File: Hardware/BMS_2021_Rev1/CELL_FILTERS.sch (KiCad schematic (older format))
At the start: 54 parts

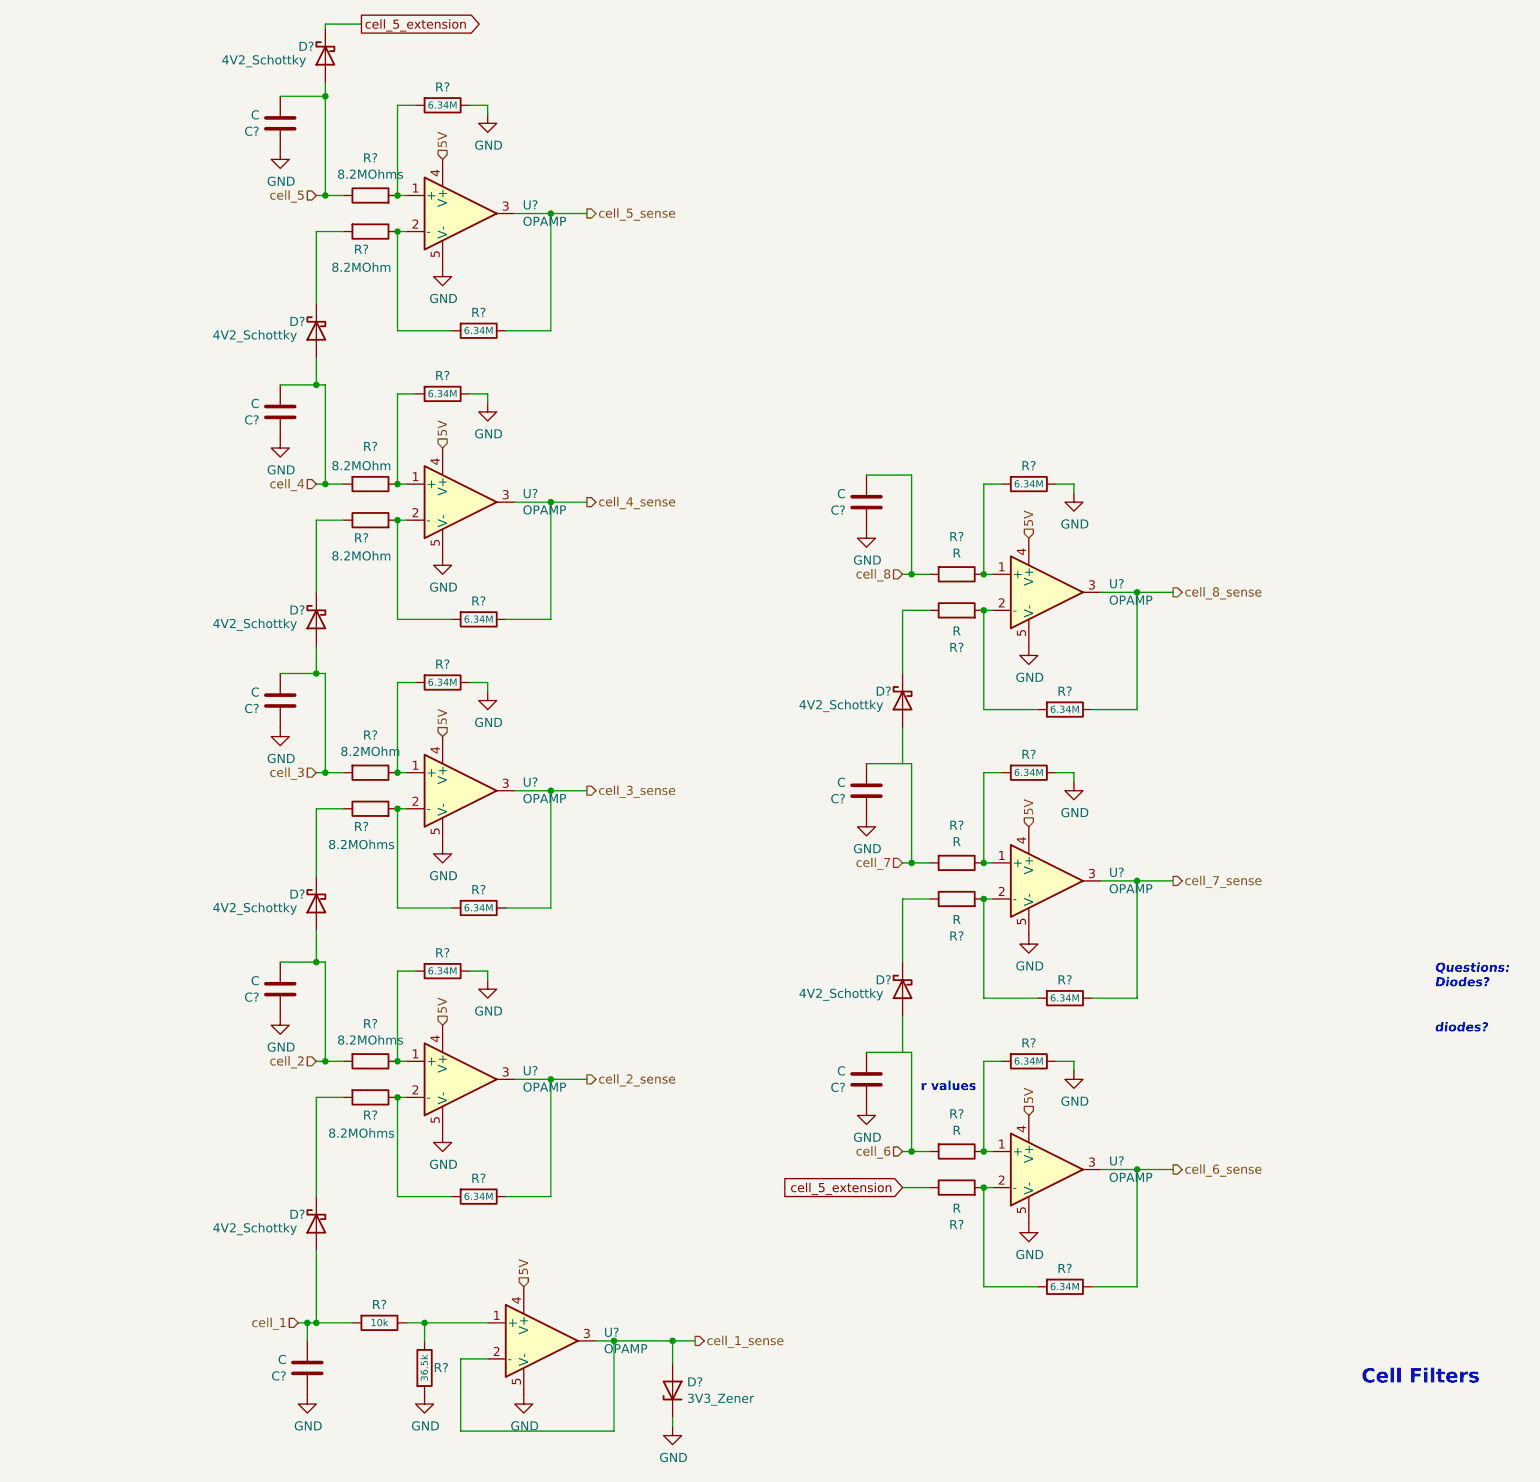
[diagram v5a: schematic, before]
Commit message: stuff added
-cellFilter IC and R values added
-MOSFET values added
-extra TIVA headers added
-currentSense R values labeled properly
-things are actually connected together this time
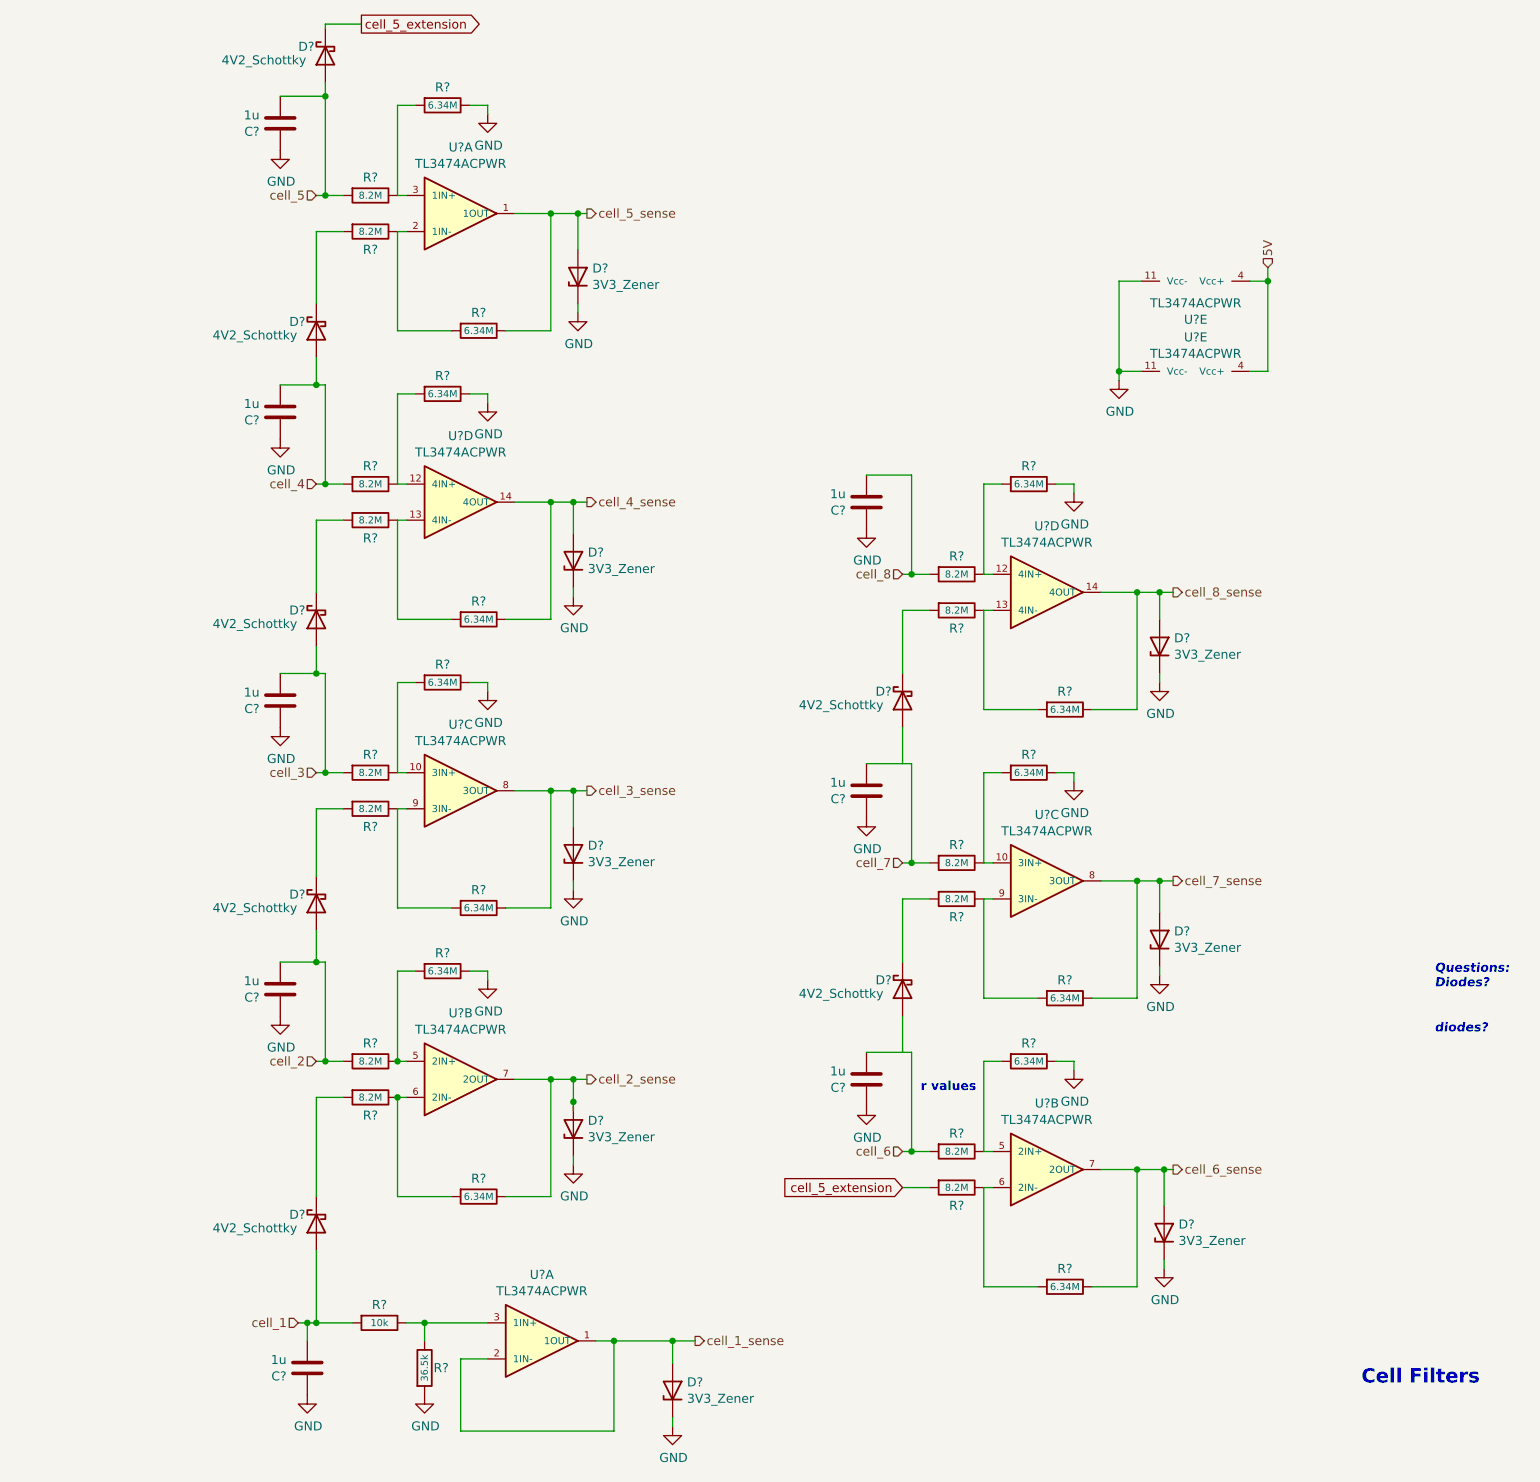
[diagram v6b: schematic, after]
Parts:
- removed C? (x7): C, symbol Device:C
- removed R? (x2): 8.2MOhms, symbol Device:R
- removed R? (x4): 8.2MOhm, symbol Device:R
- removed R? (x6): R, symbol Device:R
- removed U? (x8): OPAMP, symbol pspice:OPAMP
- added C? (x7): 1u, symbol Device:C
- added D? (x7): 3V3_Zener, symbol Device:D_Zener
- added R? (x12): 8.2M, symbol Device:R
- added U? (x10): TL3474ACPWR, symbol BMS2021_ICs:TL3474ACPWR
- C?: value C -> 1u
- R? (x2): value 8.2MOhms -> 8.2M
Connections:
- net 5V: now also U?.4 (Vcc+), U?.4 (Vcc+)
- net GND: now also C?.1, C?.1, C?.1, C?.1, C?.1, C?.1, C?.1, D?.1 (K), D?.1 (K), D?.1 (K), D?.1 (K), D?.1 (K), D?.1 (K), D?.1 (K), U?.11 (Vcc-), U?.11 (Vcc-)
- net cell_1: now also C?.2
- net cell_1_sense: now also U?.1 (1OUT), U?.2 (1IN-)
- net cell_2: now also C?.2
- net cell_2_sense: now also D?.2 (A), U?.7 (2OUT)
- net cell_3: now also C?.2, R?.2
- net cell_3_sense: now also D?.2 (A), U?.8 (3OUT)
- net cell_4: now also C?.2, R?.2
- net cell_4_sense: now also D?.2 (A), U?.14 (4OUT)
- net cell_5: now also R?.2
- net cell_5_extension: now also R?.2
- net cell_5_sense: now also D?.2 (A), U?.1 (1OUT)
- net cell_6: now also C?.2, R?.2
- net cell_6_sense: now also D?.2 (A), U?.7 (2OUT)
- net cell_7: now also C?.2, R?.2
- net cell_7_sense: now also D?.2 (A), U?.8 (3OUT)
- net cell_8: now also C?.2, R?.2
- net cell_8_sense: now also D?.2 (A), U?.14 (4OUT)
- net at R?.1, R?.2: now also U?.5 (2IN+)
- net at R?.1, R?.2: now also U?.6 (2IN-)
- net at R?.2: now also R?.1, U?.10 (3IN+) (x2)
- net at R?.2: now also R?.1, U?.9 (3IN-) (x2)
- net at D?.1 (K): now also R?.2 (x5)
- net at R?.2: now also R?.1, U?.13 (4IN-) (x2)
- net at R?.2: now also R?.1, U?.12 (4IN+) (x2)
- net at R?.2: now also R?.1, U?.2 (1IN-)
- net at R?.2: now also R?.1, U?.3 (1IN+)
- net at R?.2: now also R?.1, U?.6 (2IN-)
- net at R?.2: now also R?.1, U?.5 (2IN+)
- net at R?.1, R?.1: now also U?.3 (1IN+)

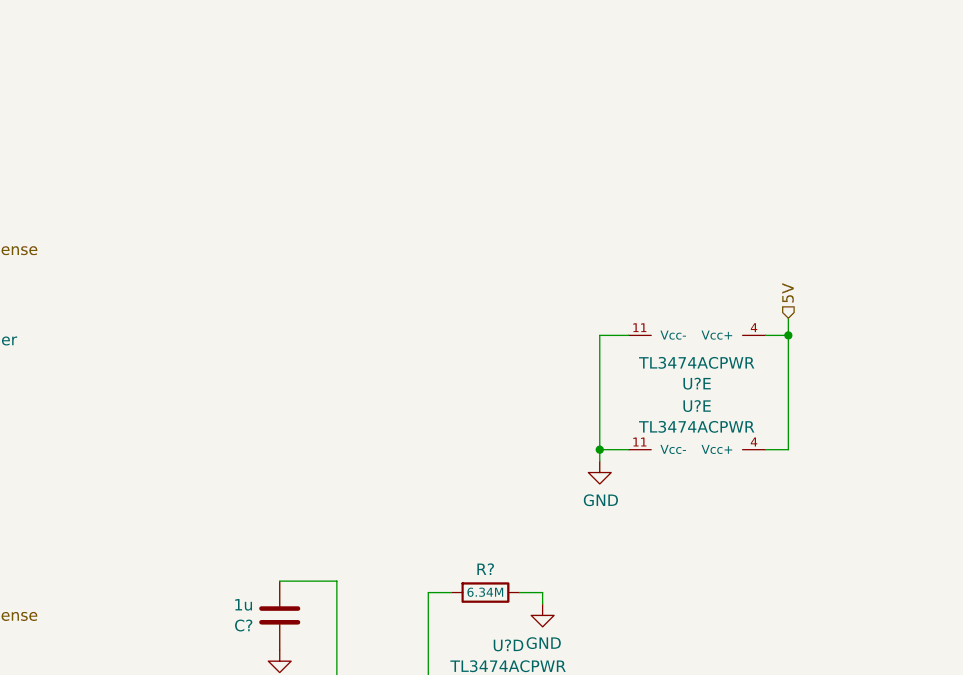
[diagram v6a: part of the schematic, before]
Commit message: added libraries to docs folder
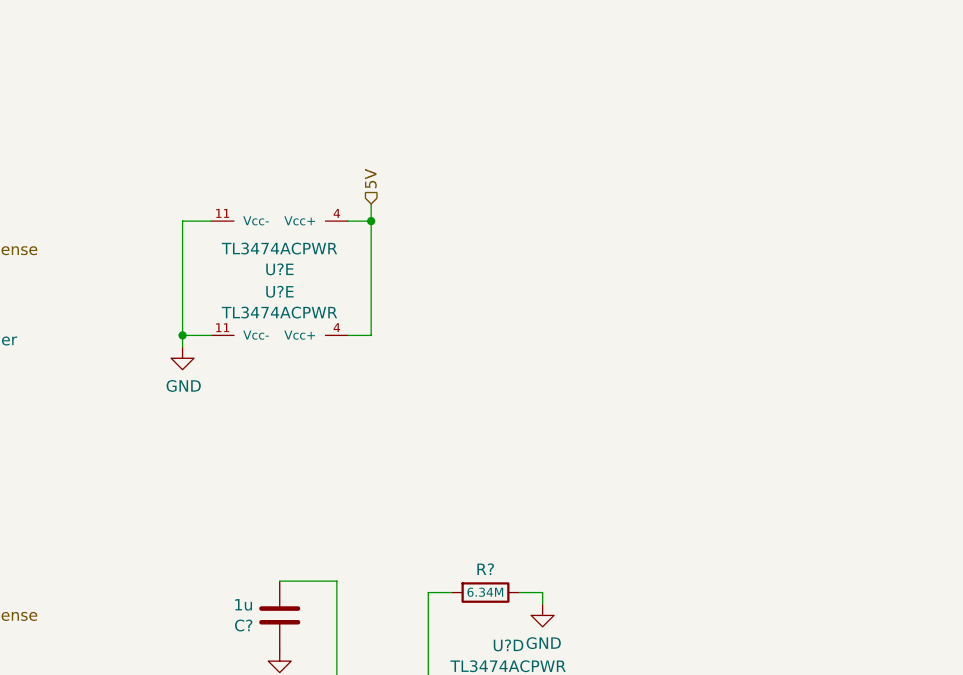
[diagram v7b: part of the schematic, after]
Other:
- moved on the sheet: U?E
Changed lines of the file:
@@
 L BMS2021_ICs:TL3474ACPWR U?
 U 5 1 5FACB20F
-P 5825 1625
-F 0 "U?" H 5825 1838 50  0000 C CNN
-F 1 "TL3474ACPWR" H 5825 1747 50  0000 C CNN
-F 2 "" H 6050 1850 50  0001 C CNN
-F 3 "https://www.digikey.com/en/products/detail/texas-instruments/TL3474ACPWR/565640" H 6050 1850 50  0001 C CNN
-	5    5825 1625
+P 4000 1125
+F 0 "U?" H 4000 1338 50  0000 C CNN
+F 1 "TL3474ACPWR" H 4000 1247 50  0000 C CNN
+F 2 "" H 4225 1350 50  0001 C CNN
+F 3 "https://www.digikey.com/en/products/detail/texas-instruments/TL3474ACPWR/565640" H 4225 1350 50  0001 C CNN
+	5    4000 1125
 	-1   0    0    1
 $EndComp
 Wire Wire Line
-	5400 2125 5400 2175
+	3575 1625 3575 1675
 Wire Wire Line
-	6125 1625 6225 1625
+	4300 1125 4400 1125
 Wire Wire Line
-	6225 1625 6225 1550
+	4400 1125 4400 1050
 $Comp
 L power:GND #PWR?
 U 1 1 5FAE6032
-P 5400 2175
-F 0 "#PWR?" H 5400 1925 50  0001 C CNN
-F 1 "GND" H 5405 2002 50  0000 C CNN
-F 2 "" H 5400 2175 50  0001 C CNN
-F 3 "" H 5400 2175 50  0001 C CNN
-	1    5400 2175
+P 3575 1675
+F 0 "#PWR?" H 3575 1425 50  0001 C CNN
+F 1 "GND" H 3580 1502 50  0000 C CNN
+F 2 "" H 3575 1675 50  0001 C CNN
+F 3 "" H 3575 1675 50  0001 C CNN
+	1    3575 1675
 	1    0    0    -1
 $EndComp
@@
 	1    0    0    -1
 $EndComp
-Text HLabel 6225 1550 1    50   Input ~ 0
+Text HLabel 4400 1050 1    50   Input ~ 0
 5V
 $Comp
@@
 L BMS2021_ICs:TL3474ACPWR U?
 U 5 1 5FB43C8D
-P 5825 2125
-F 0 "U?" H 5825 1936 50  0000 C CNN
-F 1 "TL3474ACPWR" H 5825 2027 50  0000 C CNN
-F 2 "" H 6050 2350 50  0001 C CNN
-F 3 "https://www.digikey.com/en/products/detail/texas-instruments/TL3474ACPWR/565640" H 6050 2350 50  0001 C CNN
-	5    5825 2125
+P 4000 1625
+F 0 "U?" H 4000 1436 50  0000 C CNN
+F 1 "TL3474ACPWR" H 4000 1527 50  0000 C CNN
+F 2 "" H 4225 1850 50  0001 C CNN
+F 3 "https://www.digikey.com/en/products/detail/texas-instruments/TL3474ACPWR/565640" H 4225 1850 50  0001 C CNN
+	5    4000 1625
 	-1   0    0    1
 $EndComp
 Wire Wire Line
-	6125 2125 6225 2125
+	4300 1625 4400 1625
 Wire Wire Line
-	6225 2125 6225 1625
-Connection ~ 6225 1625
+	4400 1625 4400 1125
+Connection ~ 4400 1125
 Wire Wire Line
-	5400 2125 5525 2125
+	3575 1625 3700 1625
 Wire Wire Line
-	5400 2125 5400 1625
+	3575 1625 3575 1125
 Wire Wire Line
-	5400 1625 5525 1625
-Connection ~ 5400 2125
+	3575 1125 3700 1125
+Connection ~ 3575 1625
 $Comp
 L Device:C C?

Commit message: annotated sch.
some ICs got moved around- solve later
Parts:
- removed U? (x2): TL3474ACPWR, symbol BMS2021_ICs:TL3474ACPWR
- added unit 5 of U3
- added unit 5 of U4
- gave numbers to parts that had none: 55
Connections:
- wire segments 183 -> 185
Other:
- note removed: "Questions: \nDiodes?\n"
- note removed: "diodes?"
- note removed: "r values"
- moved on the sheet: U3B, U3D, U4A, U4B, U4C, U4D
